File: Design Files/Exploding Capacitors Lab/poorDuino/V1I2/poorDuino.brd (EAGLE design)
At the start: 68.6 x 53.3 mm, 30 parts, among them IC1 LD117AS33TR, IC2 LD117AS50TR, X1 POWERSUPPLY_DC21MMX, Y2 CSTCE16M0V53-R0 16MHZ

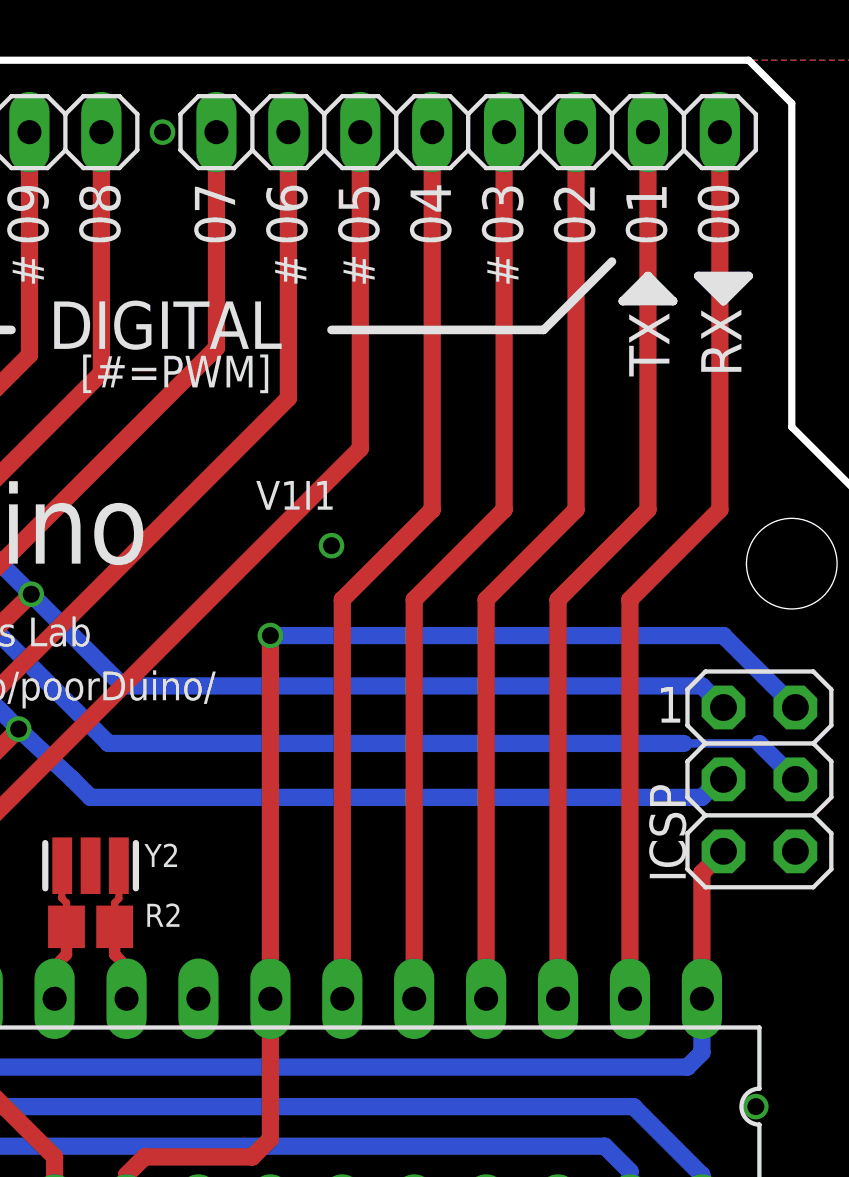
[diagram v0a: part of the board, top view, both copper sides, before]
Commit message: Differential pair routing applied to traces related to V-USB support (DIO2 and DIO4)
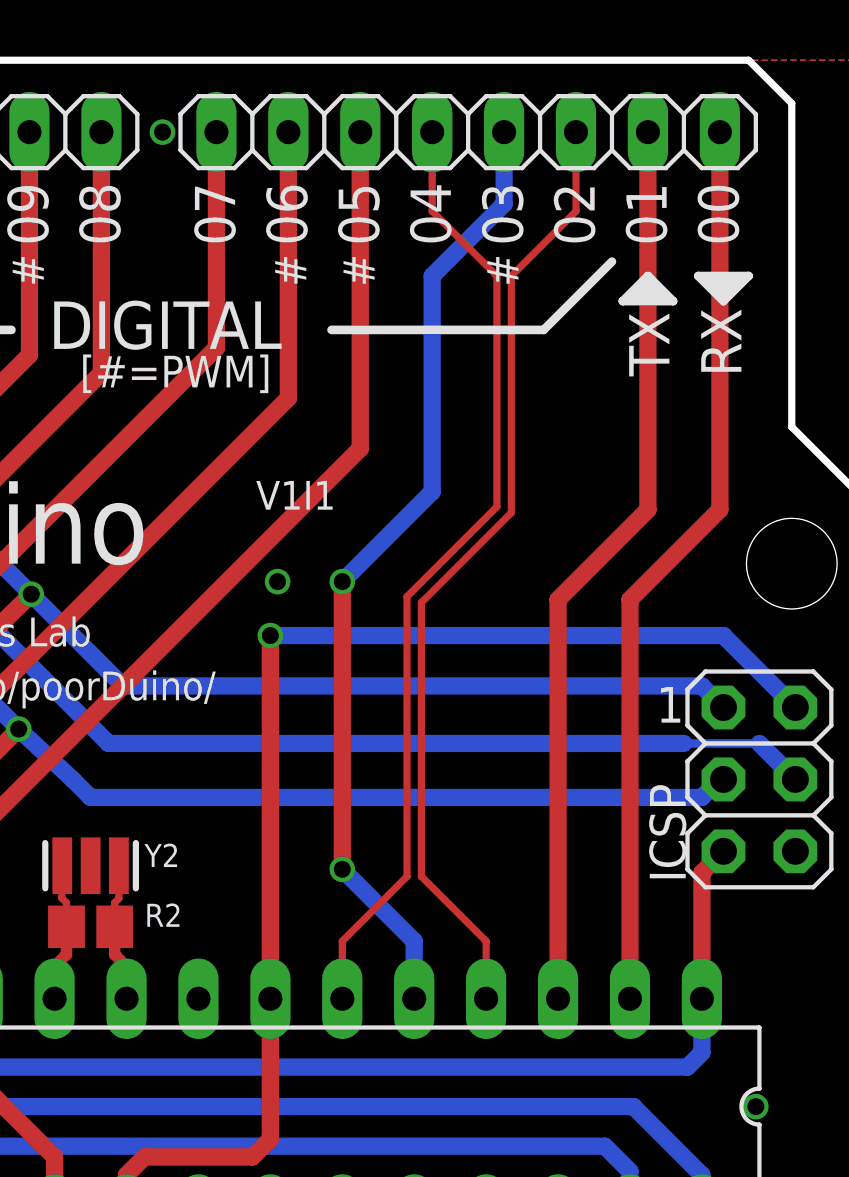
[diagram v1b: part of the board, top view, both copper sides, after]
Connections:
- net IO2 renamed USB_P
- net IO4 renamed USB_N
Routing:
- net IO3: track 31.9 -> 34.0 mm, vias 0 -> 2
- net USB_N: track 31.9 -> 33.8 mm
- net USB_P: track 31.9 -> 33.8 mm
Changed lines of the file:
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@@
 <via x="8.636" y="6.604" extent="1-16" drill="0.6"/>
 <via x="20.32" y="33.02" extent="1-16" drill="0.6"/>
-<via x="49.784" y="36.195" extent="1-16" drill="0.6"/>
+<via x="47.879" y="34.925" extent="1-16" drill="0.6"/>
 <via x="8.255" y="41.656" extent="1-16" drill="0.6"/>
 </signal>
@@
 <wire x1="17.4625" y1="47.9425" x2="17.78" y2="48.26" width="0.6096" layer="16"/>
 </signal>
-<signal name="IO2">
+<signal name="USB_P">
 <contactref element="IOL" pad="3"/>
 <contactref element="ZU4" pad="4"/>
-<wire x1="55.245" y1="20.193" x2="55.245" y2="34.29" width="0.6096" layer="1"/>
-<wire x1="55.245" y1="34.29" x2="58.42" y2="37.465" width="0.6096" layer="1"/>
-<wire x1="58.42" y1="37.465" x2="58.42" y2="50.8" width="0.6096" layer="1"/>
+<wire x1="58.42" y1="50.8" x2="58.42" y2="48.006" width="0.254" layer="1"/>
+<wire x1="58.42" y1="48.006" x2="56.134" y2="45.72" width="0.254" layer="1"/>
+<wire x1="56.134" y1="45.72" x2="56.134" y2="37.3597875" width="0.254" layer="1"/>
+<wire x1="56.134" y1="37.3597875" x2="52.959" y2="34.1847875" width="0.254" layer="1"/>
+<wire x1="52.959" y1="34.1847875" x2="52.959" y2="24.511" width="0.254" layer="1"/>
+<wire x1="52.959" y1="24.511" x2="55.245" y2="22.225" width="0.254" layer="1"/>
+<wire x1="55.245" y1="22.225" x2="55.245" y2="20.193" width="0.254" layer="1"/>
 </signal>
 <signal name="IO1">
@@
 <contactref element="ZU4" pad="5"/>
 <contactref element="IOL" pad="4"/>
-<wire x1="52.705" y1="20.193" x2="52.705" y2="34.29" width="0.6096" layer="1"/>
-<wire x1="52.705" y1="34.29" x2="55.88" y2="37.465" width="0.6096" layer="1"/>
-<wire x1="55.88" y1="37.465" x2="55.88" y2="50.8" width="0.6096" layer="1"/>
-</signal>
-<signal name="IO4">
+<wire x1="52.705" y1="20.193" x2="52.705" y2="22.225" width="0.6096" layer="16"/>
+<wire x1="52.705" y1="22.225" x2="50.165" y2="24.765" width="0.6096" layer="16"/>
+<via x="50.165" y="24.765" extent="1-16" drill="0.6"/>
+<wire x1="50.165" y1="24.765" x2="50.165" y2="34.925" width="0.6096" layer="1"/>
+<via x="50.165" y="34.925" extent="1-16" drill="0.6"/>
+<wire x1="50.165" y1="34.925" x2="53.34" y2="38.1" width="0.6096" layer="16"/>
+<wire x1="53.34" y1="38.1" x2="53.34" y2="45.72" width="0.6096" layer="16"/>
+<wire x1="53.34" y1="45.72" x2="55.88" y2="48.26" width="0.6096" layer="16"/>
+<wire x1="55.88" y1="48.26" x2="55.88" y2="50.8" width="0.6096" layer="16"/>
+</signal>
+<signal name="USB_N">
 <contactref element="IOL" pad="5"/>
 <contactref element="ZU4" pad="6"/>
-<wire x1="50.165" y1="20.193" x2="50.165" y2="34.29" width="0.6096" layer="1"/>
-<wire x1="50.165" y1="34.29" x2="53.34" y2="37.465" width="0.6096" layer="1"/>
-<wire x1="53.34" y1="37.465" x2="53.34" y2="50.8" width="0.6096" layer="1"/>
+<wire x1="53.34" y1="50.8" x2="53.34" y2="48.006" width="0.254" layer="1"/>
+<wire x1="53.34" y1="48.006" x2="55.626" y2="45.72" width="0.254" layer="1"/>
+<wire x1="55.626" y1="45.72" x2="55.626" y2="37.5702125" width="0.254" layer="1"/>
+<wire x1="55.626" y1="37.5702125" x2="52.451" y2="34.3952125" width="0.254" layer="1"/>
+<wire x1="52.451" y1="34.3952125" x2="52.451" y2="24.511" width="0.254" layer="1"/>
+<wire x1="52.451" y1="24.511" x2="50.165" y2="22.225" width="0.254" layer="1"/>
+<wire x1="50.165" y1="22.225" x2="50.165" y2="20.193" width="0.254" layer="1"/>
 </signal>
 <signal name="IO5">
